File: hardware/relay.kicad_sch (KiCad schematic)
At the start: 4 parts, among them K1 G5Q-1, U2 TCMT1100

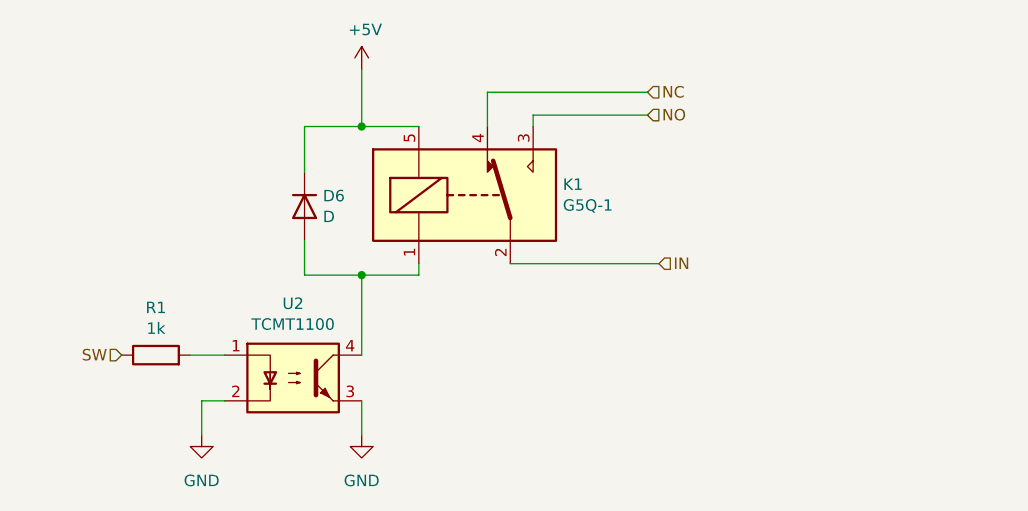
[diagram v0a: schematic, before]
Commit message: fixed current limiting resistor on optocoupler input
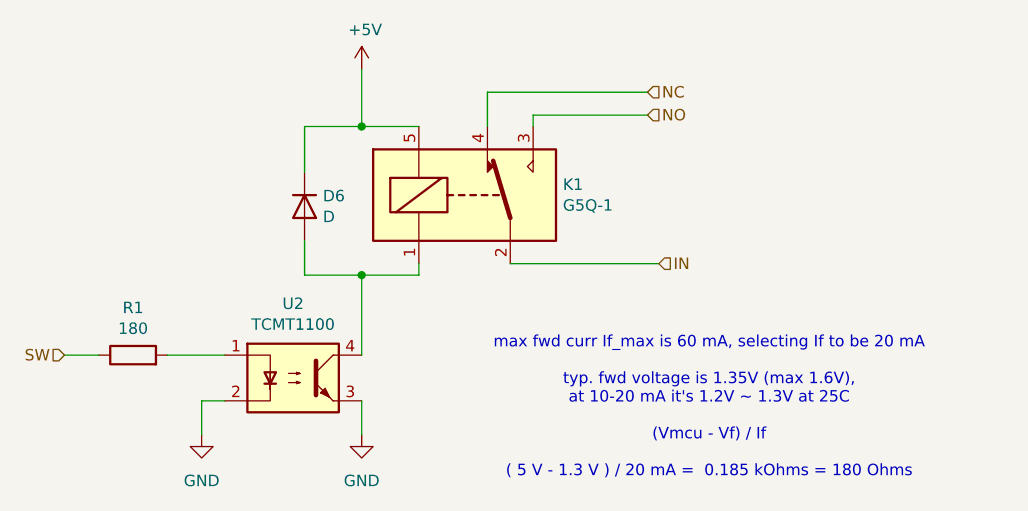
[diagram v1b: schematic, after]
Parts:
- R1: value 1k -> 180
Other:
- note added: "max fwd curr If_max is 60 mA, selecting If to be 20 mA typ. fwd voltage is 1.35V (max 1.6V), at 10-20 mA it's 1.2V ~ 1.3V at 25C (Vmcu - Vf) / If ( 5 V - 1.3 V ) / 20 mA = 0.185 kOhms = 180 Ohms"
- moved on the sheet: R1
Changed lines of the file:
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@@
+	(wire
+		(pts
+			(xy 111.76 86.36) (xy 115.57 86.36)
+		)
+		(stroke
+			(width 0)
+			(type default)
+		)
+	)
 	(wire
 		(pts
@@
 	(wire
 		(pts
-			(xy 125.73 86.36) (xy 129.54 86.36)
+			(xy 123.19 86.36) (xy 129.54 86.36)
 		)
 		(stroke
@@
 			(width 0)
 			(type default)
+		)
+	)
+	(text "max fwd curr If_max is 60 mA, selecting If to be 20 mA\n\ntyp. fwd voltage is 1.35V (max 1.6V), \nat 10-20 mA it's 1.2V ~ 1.3V at 25C\n\n(Vmcu - Vf) / If\n\n( 5 V - 1.3 V ) / 20 mA =  0.185 kOhms = 180 Ohms"
+		(exclude_from_sim no)
+		(at 183.388 92.202 0)
+		(effects
+			(font
+				(size 1.27 1.27)
+			)
 		)
 	)
@@
 	(hierarchical_label "SW"
 		(shape input)
-		(at 118.11 86.36 180)
+		(at 111.76 86.36 180)
 		(fields_autoplaced yes)
 		(effects
@@
 	(symbol
 		(lib_id "BREAD_Slice-rescue:R-OCI_UPL_1_Resistors")
-		(at 121.92 86.36 0)
+		(at 119.38 86.36 0)
 		(unit 1)
 		(exclude_from_sim no)
@@
 		(dnp no)
 		(property "Reference" "R1"
-			(at 121.92 81.1022 0)
-			(effects
-				(font
-					(size 1.27 1.27)
-				)
-			)
-		)
-		(property "Value" "1k"
-			(at 121.92 83.4136 0)
+			(at 119.38 81.1022 0)
+			(effects
+				(font
+					(size 1.27 1.27)
+				)
+			)
+		)
+		(property "Value" "180"
+			(at 119.38 83.4136 0)
 			(effects
 				(font
@@
 		)
 		(property "Footprint" "Resistor_SMD:R_1206_3216Metric_Pad1.30x1.75mm_HandSolder"
-			(at 121.92 88.138 0)
+			(at 119.38 88.138 0)
 			(effects
 				(font
@@
 		)
 		(property "Datasheet" ""
-			(at 121.92 86.36 90)
+			(at 119.38 86.36 90)
 			(effects
 				(font
@@
 		)
 		(property "Description" ""
-			(at 121.92 86.36 0)
-			(effects
-				(font
+			(at 119.38 86.36 0)
+			(effects
+				(font
